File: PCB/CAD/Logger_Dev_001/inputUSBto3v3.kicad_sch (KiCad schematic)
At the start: 30 parts, among them J4 Connector, USB-TYPE-C-16P, Q1 BC847BS, U5 AMS1117, U6 CP2102-GMR

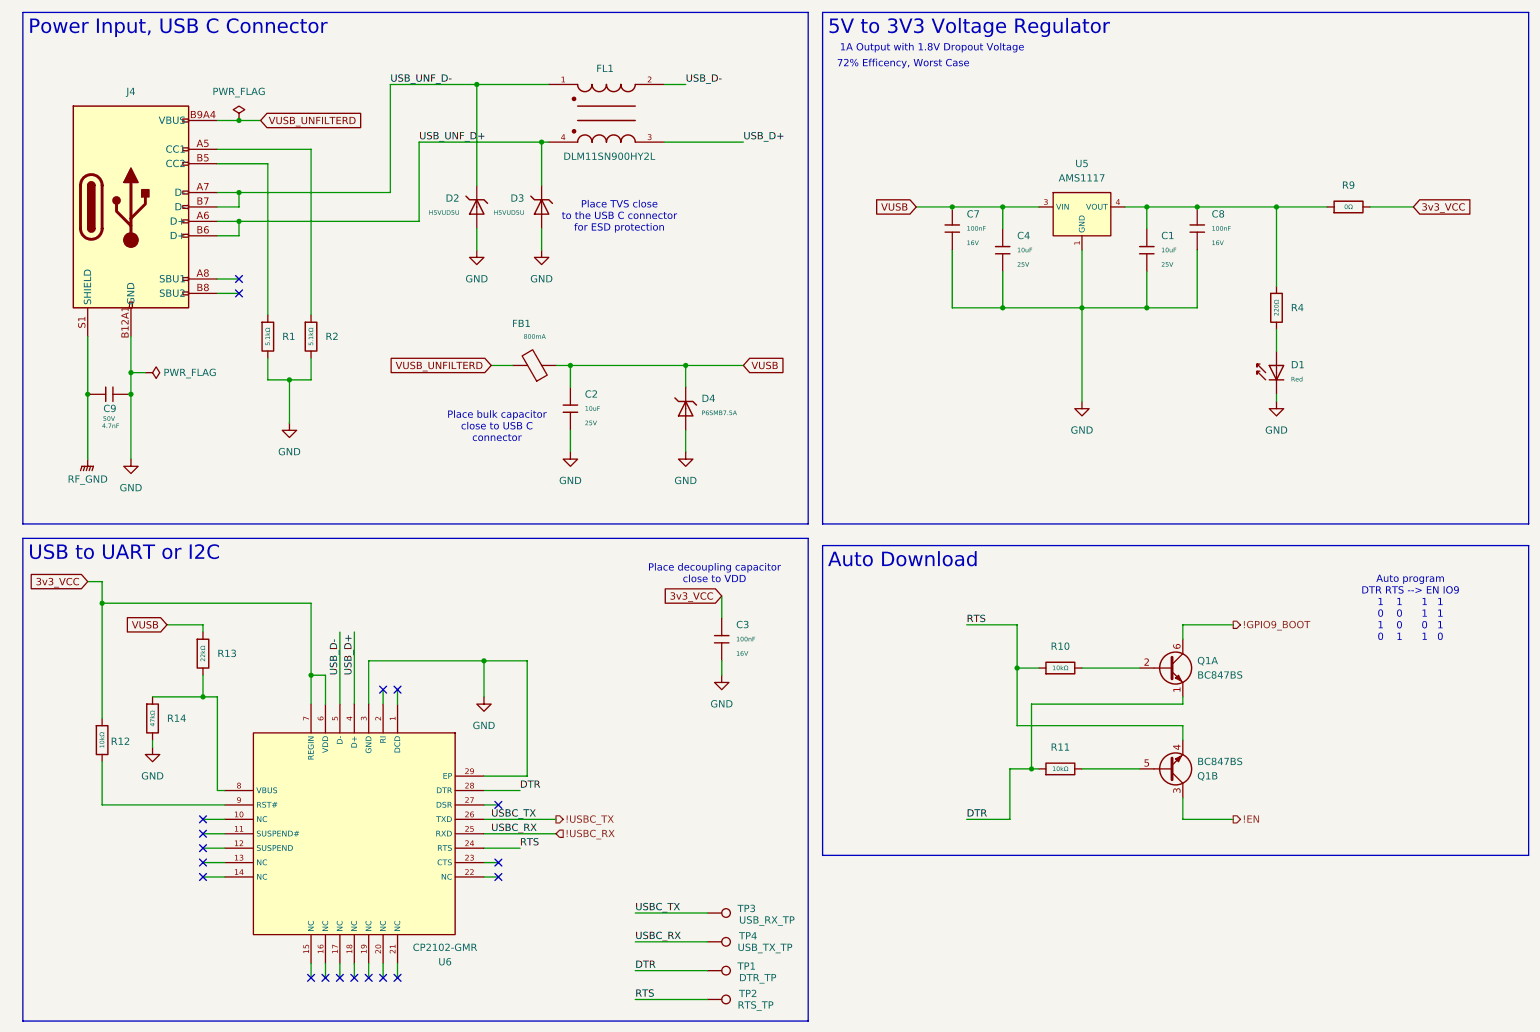
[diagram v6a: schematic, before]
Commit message: ECR Update to schematic
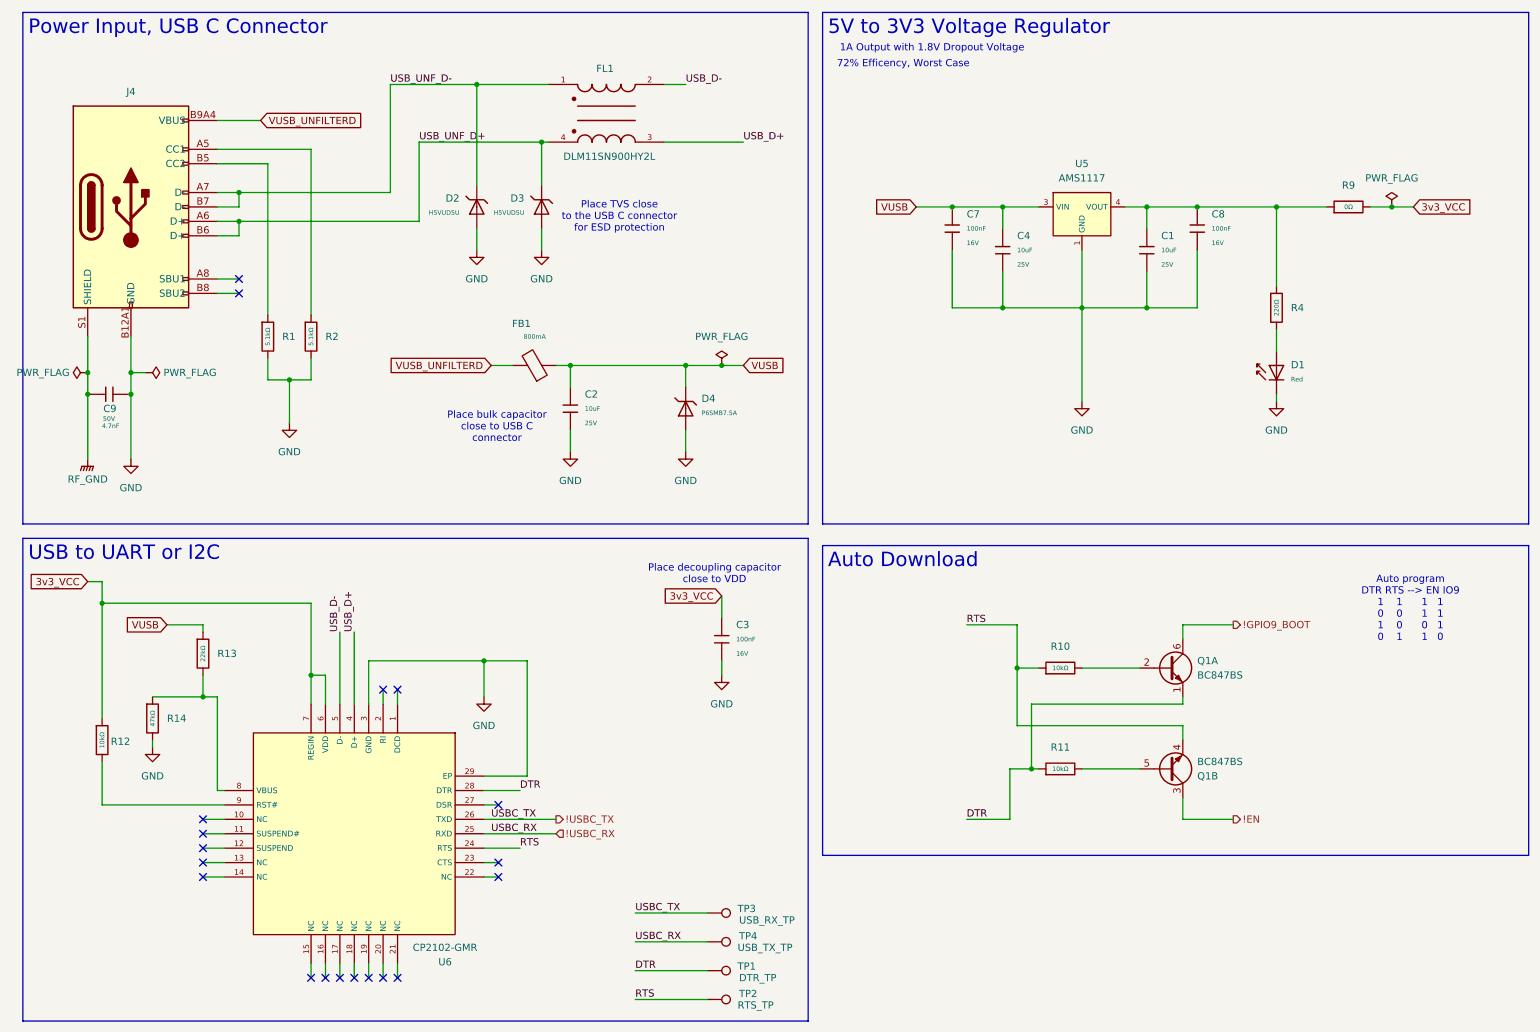
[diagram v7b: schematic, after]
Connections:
- net RF_GND is gone; now on net GND: C9.1, J4.S1 (SHIELD)
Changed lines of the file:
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@@
 	)
 	(junction
+		(at 257.81 49.53)
+		(diameter 0)
+		(color 0 0 0 0)
+	)
+	(junction
 		(at 27.94 82.55)
 		(diameter 0)
@@
 	)
 	(junction
+		(at 27.94 78.74)
+		(diameter 0)
+		(color 0 0 0 0)
+	)
+	(junction
 		(at 189.23 67.31)
 		(diameter 0)
@@
 	)
 	(junction
+		(at 139.7 77.47)
+		(diameter 0)
+		(color 0 0 0 0)
+	)
+	(junction
 		(at 48.26 135.89)
 		(diameter 0)
@@
 	)
 	(junction
-		(at 54.61 34.29)
-		(diameter 0)
-		(color 0 0 0 0)
-	)
-	(junction
 		(at 63.5 80.01)
 		(diameter 0)
@@
 	(wire
 		(pts
-			(xy 254 49.53) (xy 261.62 49.53)
+			(xy 254 49.53) (xy 257.81 49.53)
 		)
 		(stroke
@@
 	(wire
 		(pts
-			(xy 54.61 34.29) (xy 58.42 34.29)
-		)
-		(stroke
-			(width 0)
-			(type default)
-		)
-	)
-	(wire
-		(pts
 			(xy 237.49 49.53) (xy 246.38 49.53)
 		)
@@
 	(wire
 		(pts
+			(xy 257.81 49.53) (xy 261.62 49.53)
+		)
+		(stroke
+			(width 0)
+			(type default)
+		)
+	)
+	(wire
+		(pts
 			(xy 67.31 182.88) (xy 67.31 185.42)
 		)
@@
 	(wire
 		(pts
-			(xy 133.35 77.47) (xy 143.51 77.47)
+			(xy 133.35 77.47) (xy 139.7 77.47)
 		)
 		(stroke
@@
 	(wire
 		(pts
-			(xy 74.93 124.46) (xy 74.93 137.16)
+			(xy 35.56 78.74) (xy 38.1 78.74)
 		)
 		(stroke
@@
 	(wire
 		(pts
-			(xy 35.56 78.74) (xy 38.1 78.74)
+			(xy 237.49 82.55) (xy 237.49 83.82)
 		)
 		(stroke
@@
 	(wire
 		(pts
-			(xy 237.49 82.55) (xy 237.49 83.82)
+			(xy 74.93 124.46) (xy 74.93 137.16)
 		)
 		(stroke
@@
 	(wire
 		(pts
+			(xy 27.94 78.74) (xy 27.94 82.55)
+		)
+		(stroke
+			(width 0)
+			(type default)
+		)
+	)
+	(wire
+		(pts
 			(xy 191.77 123.19) (xy 191.77 130.81)
 		)
@@
 	(wire
 		(pts
-			(xy 50.8 34.29) (xy 54.61 34.29)
+			(xy 50.8 34.29) (xy 58.42 34.29)
 		)
 		(stroke
@@
 	(wire
 		(pts
+			(xy 72.39 124.46) (xy 72.39 137.16)
+		)
+		(stroke
+			(width 0)
+			(type default)
+		)
+	)
+	(wire
+		(pts
 			(xy 190.5 148.59) (xy 190.5 157.48)
 		)
@@
 	(wire
 		(pts
-			(xy 72.39 124.46) (xy 72.39 137.16)
+			(xy 139.7 77.47) (xy 143.51 77.47)
 		)
 		(stroke
@@
 	(wire
 		(pts
-			(xy 27.94 72.39) (xy 27.94 82.55)
+			(xy 27.94 72.39) (xy 27.94 78.74)
 		)
 		(stroke
@@
 	)
 	(label "USB_D+"
-		(at 74.93 132.08 90)
+		(at 74.93 124.46 90)
 		(effects
 			(font
@@
 	)
 	(label "USB_D-"
-		(at 72.39 132.08 90)
+		(at 72.39 124.46 90)
 		(effects
 			(font
@@
 	)
 	(symbol
+		(lib_name "PWR_FLAG_1")
+		(lib_id "power:PWR_FLAG")
+		(at 27.94 78.74 90)
+		(unit 1)
+		(exclude_from_sim no)
+		(in_bom yes)
+		(on_board yes)
+		(dnp no)
+		(property "Reference" "#FLG03"
+			(at 26.035 78.74 0)
+			(effects
+				(font
+					(size 1.27 1.27)
+				)
+				(hide yes)
+			)
+		)
+		(property "Value" "PWR_FLAG"
+			(at 20.066 78.74 90)
+			(effects
+				(font
+					(size 1.27 1.27)
+				)
+			)
+		)
+		(property "Footprint" ""
+			(at 27.94 78.74 0)
+			(effects
+				(font
+					(size 1.27 1.27)
+				)
+				(hide yes)
+			)
+		)
+		(property "Datasheet" "~"
+			(at 27.94 78.74 0)
+			(effects
+				(font
+					(size 1.27 1.27)
+				)
+				(hide yes)
+			)
+		)
+		(property "Description" "Special symbol for telling ERC where power comes from"
+			(at 27.94 78.74 0)
+			(effects
+				(font
+					(size 1.27 1.27)
+				)
+				(hide yes)
+			)
+		)
+		(pin "1"
+		)
+		(instances
+			(project "Logger_Dev_001"
+				(path "/9546b831-c7ee-4f40-8993-5fd5a38d4078/588c330f-0a28-4ec5-8e7c-c377534893c3"
+					(reference "#FLG03")
+					(unit 1)
+				)
+			)
+		)
+	)
+	(symbol
 		(lib_id "PCM_JLCPCB-Extended:Connector, USB-TYPE-C-16P")
 		(at 35.56 49.53 0)
@@
 	)
 	(symbol
+		(lib_id "power:PWR_FLAG")
+		(at 257.81 49.53 0)
+		(unit 1)
+		(exclude_from_sim no)
+		(in_bom yes)
+		(on_board yes)
+		(dnp no)
+		(fields_autoplaced yes)
+		(property "Reference" "#FLG05"
+			(at 257.81 47.625 0)
+			(effects
+				(font
+					(size 1.27 1.27)
+				)
+				(hide yes)
+			)
+		)
+		(property "Value" "PWR_FLAG"
+			(at 257.81 44.45 0)
+			(effects
+				(font
+					(size 1.27 1.27)
+				)
+			)
+		)
+		(property "Footprint" ""
+			(at 257.81 49.53 0)
+			(effects
+				(font
+					(size 1.27 1.27)
+				)
+				(hide yes)
+			)
+		)
+		(property "Datasheet" "~"
+			(at 257.81 49.53 0)
+			(effects
+				(font
+					(size 1.27 1.27)
+				)
+				(hide yes)
+			)
+		)
+		(property "Description" "Special symbol for telling ERC where power comes from"
+			(at 257.81 49.53 0)
+			(effects
+				(font
+					(size 1.27 1.27)
+				)
+				(hide yes)
+			)
+		)
+		(pin "1"
+		)
+		(instances
+			(project "Logger_Dev_001"
+				(path "/9546b831-c7ee-4f40-8993-5fd5a38d4078/588c330f-0a28-4ec5-8e7c-c377534893c3"
+					(reference "#FLG05")
+					(unit 1)
+				)
+			)
+		)
+	)
+	(symbol
 		(lib_id "power:GND")
 		(at 96.52 57.15 0)
@@
 	(symbol
 		(lib_id "power:PWR_FLAG")
-		(at 54.61 34.29 0)
+		(at 139.7 77.47 0)
 		(unit 1)
 		(exclude_from_sim no)
@@
 		(fields_autoplaced yes)
 		(property "Reference" "#FLG01"
-			(at 54.61 32.385 0)
+			(at 139.7 75.565 0)
 			(effects
 				(font
@@
 		)
 		(property "Value" "PWR_FLAG"
-			(at 54.61 29.21 0)
+			(at 139.7 72.39 0)
 			(effects
 				(font
@@
 		)
 		(property "Footprint" ""
-			(at 54.61 34.29 0)
+			(at 139.7 77.47 0)
 			(effects
 				(font
@@
 		)
 		(property "Datasheet" "~"
-			(at 54.61 34.29 0)
+			(at 139.7 77.47 0)
 			(effects
 				(font
@@
 		)
 		(property "Description" "Special symbol for telling ERC where power comes from"
-			(at 54.61 34.29 0)
+			(at 139.7 77.47 0)
 			(effects
 				(font
@@
 		)
 		(instances
-			(project ""
+			(project "Logger_Dev_001"
 				(path "/9546b831-c7ee-4f40-8993-5fd5a38d4078/588c330f-0a28-4ec5-8e7c-c377534893c3"
 					(reference "#FLG01")
@@
 	)
 	(symbol
+		(lib_name "PWR_FLAG_1")
 		(lib_id "power:PWR_FLAG")
 		(at 38.1 78.74 270)

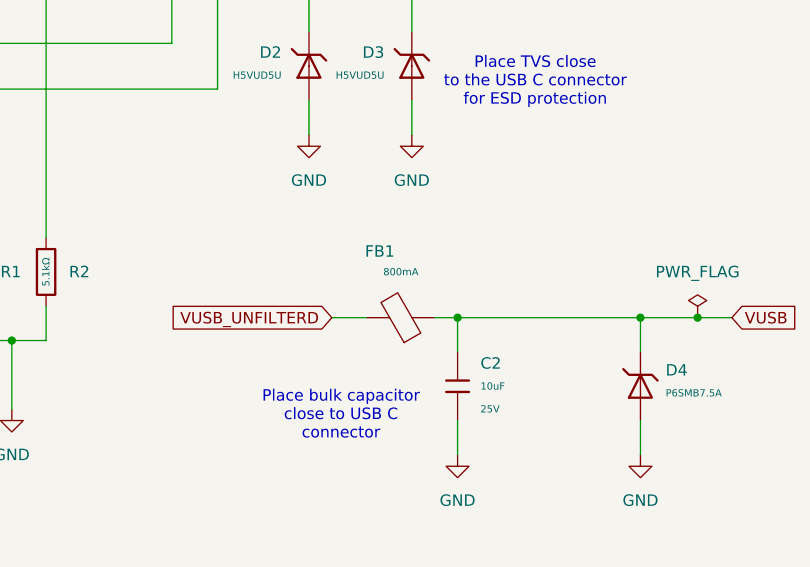
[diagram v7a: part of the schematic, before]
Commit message: Update via size to reduce cost
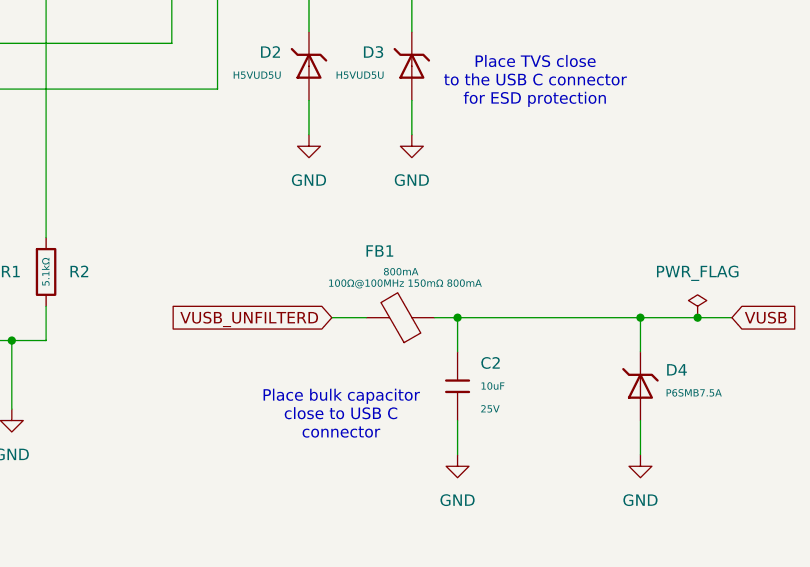
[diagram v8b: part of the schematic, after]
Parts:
- FB1: value ~ -> 100Ω@100MHz 150mΩ 800mA
- FL1: LCSC (none) -> C161089
- TP1, TP2, TP3, TP4: now left out of the parts list
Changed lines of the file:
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@@
 		(unit 1)
 		(exclude_from_sim no)
-		(in_bom yes)
+		(in_bom no)
 		(on_board yes)
 		(dnp no)
@@
 		(unit 1)
 		(exclude_from_sim no)
-		(in_bom yes)
+		(in_bom no)
 		(on_board yes)
 		(dnp no)
@@
 		(unit 1)
 		(exclude_from_sim no)
-		(in_bom yes)
+		(in_bom no)
 		(on_board yes)
 		(dnp no)
@@
 			)
 		)
-		(property "Datasheet" ""
+		(property "Datasheet" "https://jlcpcb.com/api/file/downloadByFileSystemAccessId/8588884046855720960"
 			(at 119.38 33.02 0)
 			(effects
@@
 			)
 		)
-		(property "Description" ""
+		(property "Description" "-40℃~+85℃ 1.38Ω 100MΩ 100mA 12.5V 2 5V 90Ω@100MHz SMD-4P,1.2x1mm Common Mode Filters ROHS"
 			(at 119.38 33.02 0)
 			(effects
@@
 			)
 		)
+		(property "LCSC" "C161089"
+			(at 119.38 33.02 0)
+			(effects
+				(font
+					(size 1.27 1.27)
+				)
+				(hide yes)
+			)
+		)
 		(pin "1"
 		)
@@
 		(unit 1)
 		(exclude_from_sim no)
-		(in_bom yes)
+		(in_bom no)
 		(on_board yes)
 		(dnp no)
@@
 			)
 		)
-		(property "Value" "~"
-			(at 106.7308 69.85 90)
+		(property "Value" "100Ω@100MHz 150mΩ 800mA"
+			(at 107.188 73.66 90)
 			(effects
 				(font
